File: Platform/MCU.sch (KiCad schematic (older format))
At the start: 33 parts, among them J10 Conn_01x05, J11 Aardvark Header SPI, J12 Aardvark Header I2C, J13 ESP8266_CONN, J14 Aardvark Header I2C, J4 Conn_01x05, J5 GPIO Drive, J6 Debug Hdr, J7 Conn_01x05, J9 Conn_01x05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

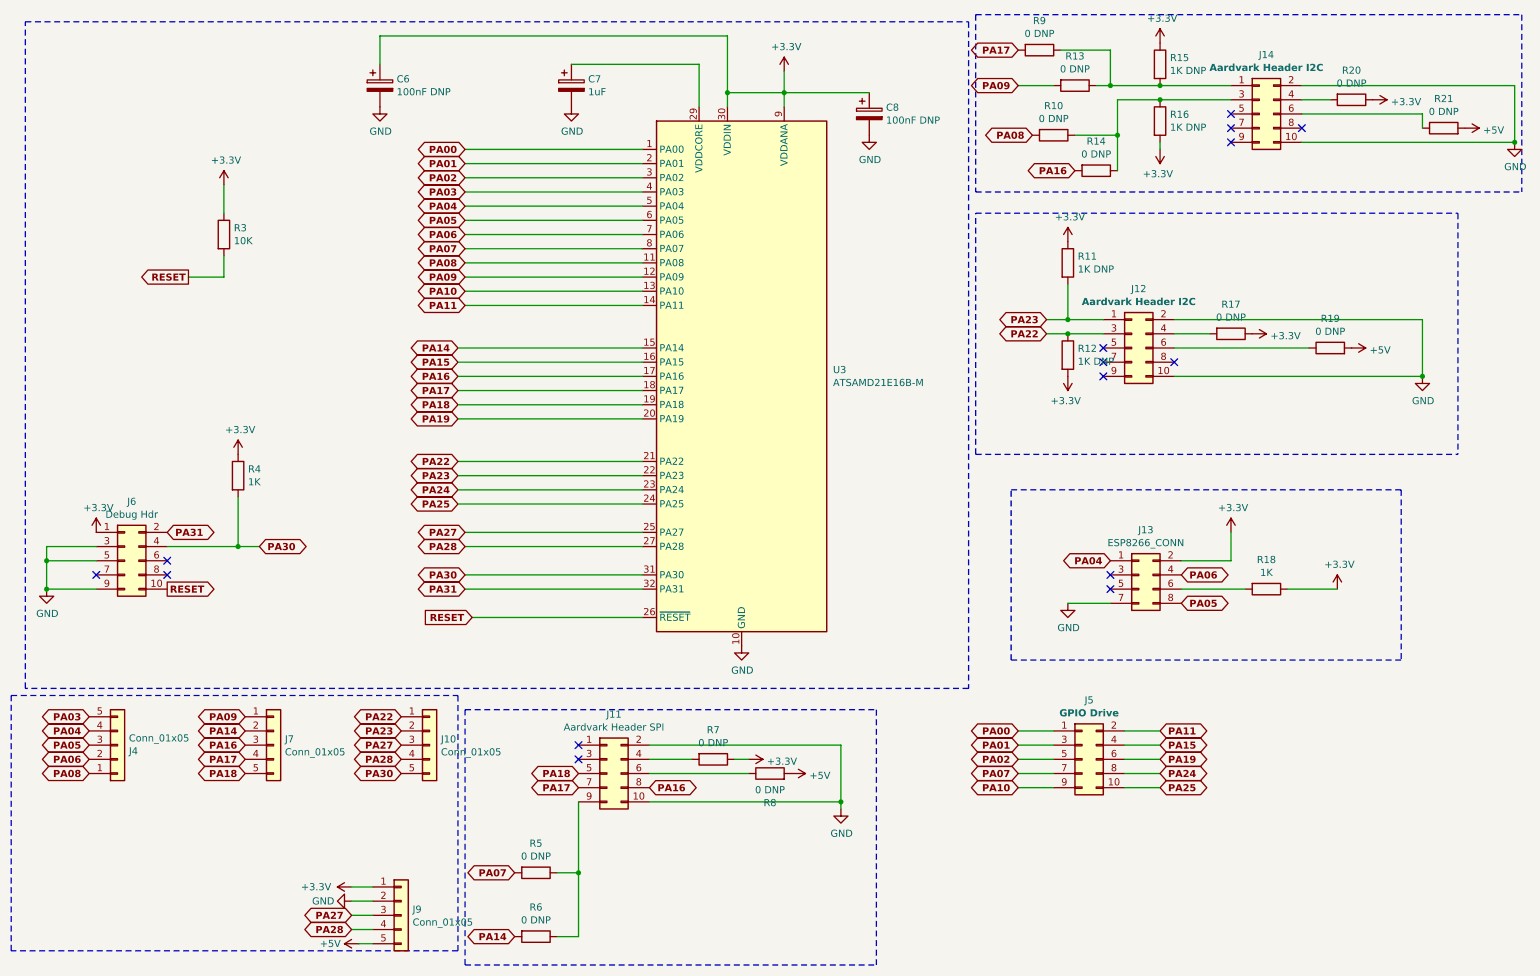
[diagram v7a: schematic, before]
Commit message: updated the platform schematic.
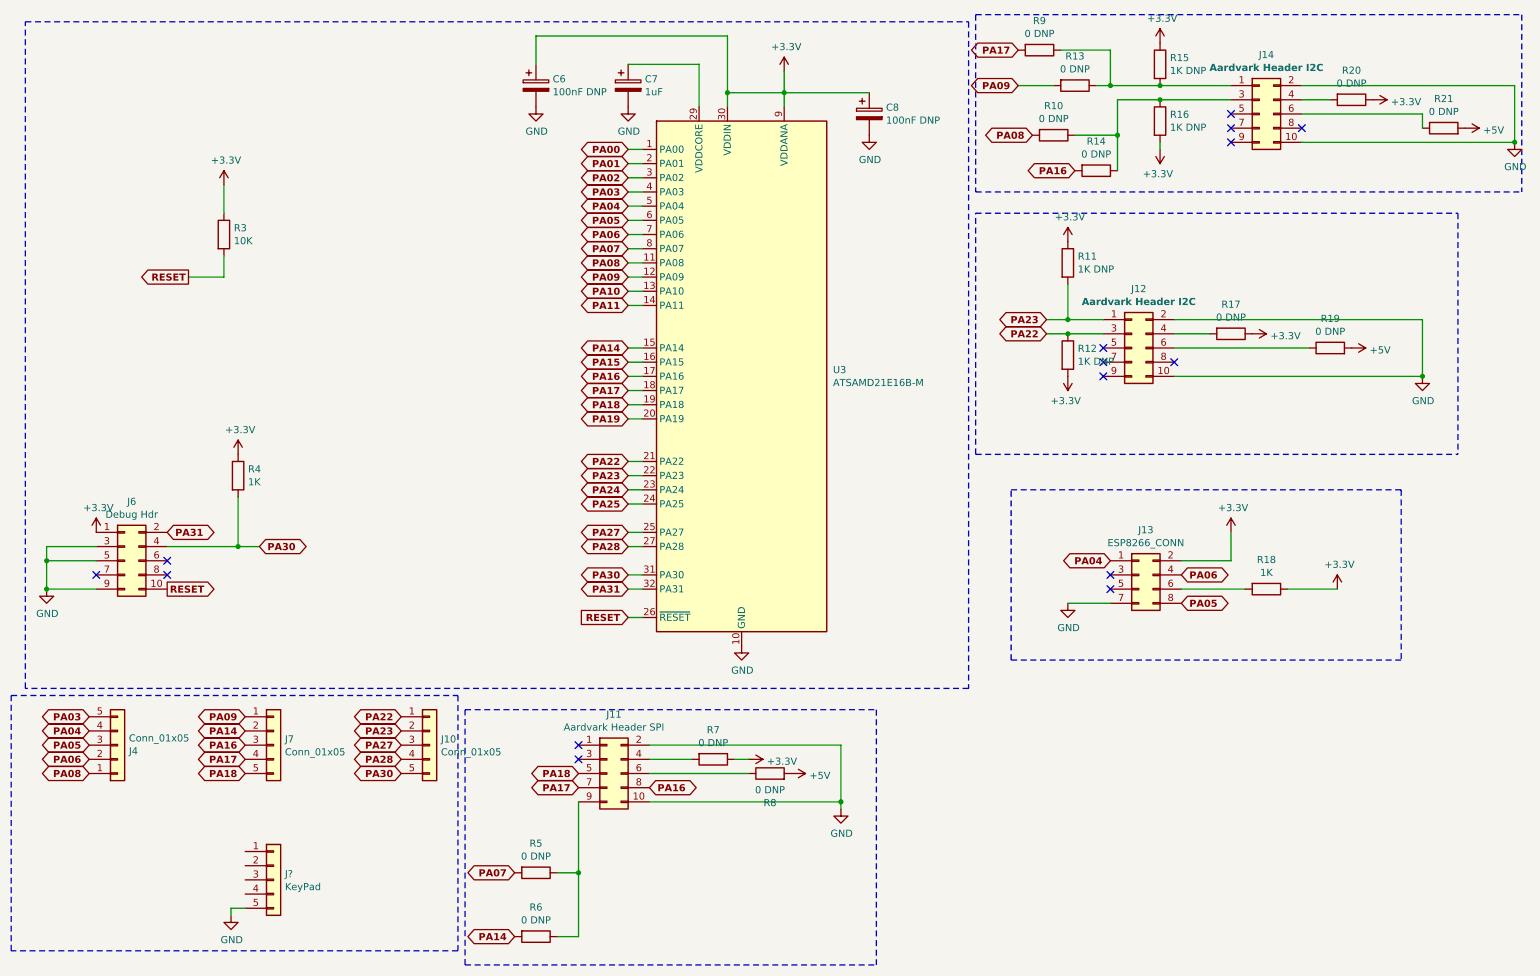
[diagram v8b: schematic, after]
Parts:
- removed J5: GPIO Drive, symbol Connector_Generic:Conn_02x05_Odd_Even
- removed J9: Conn_01x05, symbol Connector_Generic:Conn_01x05
- added J?: KeyPad, symbol Connector_Generic:Conn_01x05
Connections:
- net GND: now also J?.5 (Pin_5)
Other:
- moved on the sheet: C6, C7
